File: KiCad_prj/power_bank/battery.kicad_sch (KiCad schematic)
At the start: 27 parts, among them Q1 IRFR5305, Q2 IRFR4105, Q4 BC847BS, Q5 BC857BS, U1 LM317, U3 LM337

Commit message: power_bank: dokonceny navrh schema
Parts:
- renumbered C4 to C14, C3 to C15, C2 to C16, C1 to C17, C5 to C18, C6 to C19, D1 to D2, Q4 to Q1, Q5 to Q2, Q1 to Q3, Q2 to Q4, R1 to R10, R6 to R11, R5 to R12, R9 to R13, R4 to R14, R10 to R15, R2 to R16, R8 to R17, R7 to R18, R3 to R9, RV2 to RV1, RV1 to RV2, U1 to U4
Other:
- title: (none) -> ${TITLE}
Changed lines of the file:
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@@
 	(generator_version "9.0")
 	(paper "A4")
+	(title_block
+		(title "${TITLE}")
+		(date "2026-01-15")
+		(rev "${REVISION}")
+		(comment 1 "${DESCR}")
+	)
 	(junction
 		(at 106.68 107.95)
@@
 		(dnp no)
 		(fields_autoplaced yes)
-		(property "Reference" "R7"
+		(property "Reference" "R18"
 			(at 177.8 125.7299 0)
 			(effects
@@
 			(project "power_bank"
 				(path "/43391614-883f-49dc-a949-0152c58fc2fa/9147f2e0-7dcc-462c-aa60-5310dabd00a6"
-					(reference "R7")
+					(reference "R18")
 					(unit 1)
 				)
@@
 		(dnp no)
 		(fields_autoplaced yes)
-		(property "Reference" "D1"
+		(property "Reference" "D2"
 			(at 219.71 91.4399 90)
 			(effects
@@
 			(project ""
 				(path "/43391614-883f-49dc-a949-0152c58fc2fa/9147f2e0-7dcc-462c-aa60-5310dabd00a6"
-					(reference "D1")
+					(reference "D2")
 					(unit 1)
 				)
@@
 		(dnp no)
 		(fields_autoplaced yes)
-		(property "Reference" "R3"
+		(property "Reference" "R9"
 			(at 106.68 78.74 90)
 			(effects
@@
 			(project "power_bank"
 				(path "/43391614-883f-49dc-a949-0152c58fc2fa/9147f2e0-7dcc-462c-aa60-5310dabd00a6"
-					(reference "R3")
+					(reference "R9")
 					(unit 1)
 				)
@@
 		(dnp no)
 		(fields_autoplaced yes)
-		(property "Reference" "R10"
+		(property "Reference" "R15"
 			(at 168.91 54.6099 0)
 			(effects
@@
 			(project "power_bank"
 				(path "/43391614-883f-49dc-a949-0152c58fc2fa/9147f2e0-7dcc-462c-aa60-5310dabd00a6"
-					(reference "R10")
+					(reference "R15")
 					(unit 1)
 				)
@@
 		(on_board yes)
 		(dnp no)
-		(property "Reference" "Q4"
+		(property "Reference" "Q1"
 			(at 154.94 68.5801 0)
 			(effects
@@
 			(project ""
 				(path "/43391614-883f-49dc-a949-0152c58fc2fa/9147f2e0-7dcc-462c-aa60-5310dabd00a6"
-					(reference "Q4")
+					(reference "Q1")
 					(unit 1)
 				)
@@
 		(on_board yes)
 		(dnp no)
-		(property "Reference" "C5"
+		(property "Reference" "C18"
 			(at 128.27 72.3899 0)
 			(effects
@@
 			(project "power_bank"
 				(path "/43391614-883f-49dc-a949-0152c58fc2fa/9147f2e0-7dcc-462c-aa60-5310dabd00a6"
-					(reference "C5")
+					(reference "C18")
 					(unit 1)
 				)
@@
 		(dnp no)
 		(fields_autoplaced yes)
-		(property "Reference" "U1"
+		(property "Reference" "U4"
 			(at 95.25 93.98 0)
 			(effects
@@
 			(project "power_bank"
 				(path "/43391614-883f-49dc-a949-0152c58fc2fa/9147f2e0-7dcc-462c-aa60-5310dabd00a6"
-					(reference "U1")
+					(reference "U4")
 					(unit 1)
 				)
@@
 		(dnp no)
 		(fields_autoplaced yes)
-		(property "Reference" "R1"
+		(property "Reference" "R10"
 			(at 106.68 93.98 90)
 			(effects
@@
 			(project "power_bank"
 				(path "/43391614-883f-49dc-a949-0152c58fc2fa/9147f2e0-7dcc-462c-aa60-5310dabd00a6"
-					(reference "R1")
+					(reference "R10")
 					(unit 1)
 				)
@@
 		(dnp no)
 		(fields_autoplaced yes)
-		(property "Reference" "C4"
+		(property "Reference" "C14"
 			(at 78.74 110.4899 0)
 			(effects
@@
 			(project "power_bank"
 				(path "/43391614-883f-49dc-a949-0152c58fc2fa/9147f2e0-7dcc-462c-aa60-5310dabd00a6"
-					(reference "C4")
+					(reference "C14")
 					(unit 1)
 				)
@@
 		(dnp no)
 		(fields_autoplaced yes)
-		(property "Reference" "C1"
+		(property "Reference" "C17"
 			(at 99.06 110.4899 0)
 			(effects
@@
 			(project "power_bank"
 				(path "/43391614-883f-49dc-a949-0152c58fc2fa/9147f2e0-7dcc-462c-aa60-5310dabd00a6"
-					(reference "C1")
+					(reference "C17")
 					(unit 1)
 				)
@@
 		(dnp no)
 		(fields_autoplaced yes)
-		(property "Reference" "R2"
+		(property "Reference" "R16"
 			(at 168.91 125.7299 0)
 			(effects
@@
 			(project ""
 				(path "/43391614-883f-49dc-a949-0152c58fc2fa/9147f2e0-7dcc-462c-aa60-5310dabd00a6"
-					(reference "R2")
+					(reference "R16")
 					(unit 1)
 				)
@@
 		(on_board yes)
 		(dnp no)
-		(property "Reference" "C6"
+		(property "Reference" "C19"
 			(at 128.27 110.4899 0)
 			(effects
@@
 			(project "power_bank"
 				(path "/43391614-883f-49dc-a949-0152c58fc2fa/9147f2e0-7dcc-462c-aa60-5310dabd00a6"
-					(reference "C6")
+					(reference "C19")
 					(unit 1)
 				)
@@
 		(dnp no)
 		(fields_autoplaced yes)
-		(property "Reference" "R9"
+		(property "Reference" "R13"
 			(at 160.02 54.6099 0)
 			(effects
@@
 			(project "power_bank"
 				(path "/43391614-883f-49dc-a949-0152c58fc2fa/9147f2e0-7dcc-462c-aa60-5310dabd00a6"
-					(reference "R9")
+					(reference "R13")
 					(unit 1)
 				)
@@
 		(dnp no)
 		(fields_autoplaced yes)
-		(property "Reference" "R6"
+		(property "Reference" "R11"
 			(at 113.03 80.0099 0)
 			(effects
@@
 			(project "power_bank"
 				(path "/43391614-883f-49dc-a949-0152c58fc2fa/9147f2e0-7dcc-462c-aa60-5310dabd00a6"
-					(reference "R6")
+					(reference "R11")
 					(unit 1)
 				)
@@
 		(on_board yes)
 		(dnp no)
-		(property "Reference" "Q5"
+		(property "Reference" "Q2"
 			(at 177.8 114.2999 0)
 			(effects
@@
 			(project ""
 				(path "/43391614-883f-49dc-a949-0152c58fc2fa/9147f2e0-7dcc-462c-aa60-5310dabd00a6"
-					(reference "Q5")
+					(reference "Q2")
 					(unit 2)
 				)
@@
 		(dnp no)
 		(fields_autoplaced yes)
-		(property "Reference" "R5"
+		(property "Reference" "R12"
 			(at 113.03 102.8699 0)
 			(effects
@@
 			(project "power_bank"
 				(path "/43391614-883f-49dc-a949-0152c58fc2fa/9147f2e0-7dcc-462c-aa60-5310dabd00a6"
-					(reference "R5")
+					(reference "R12")
 					(unit 1)
 				)
@@
 		(on_board yes)
 		(dnp no)
-		(property "Reference" "Q4"
+		(property "Reference" "Q1"
 			(at 177.8 68.5801 0)
 			(effects
@@
 			(project ""
 				(path "/43391614-883f-49dc-a949-0152c58fc2fa/9147f2e0-7dcc-462c-aa60-5310dabd00a6"
-					(reference "Q4")
+					(reference "Q1")
 					(unit 2)
 				)
@@
 		(dnp no)
 		(fields_autoplaced yes)
-		(property "Reference" "R8"
+		(property "Reference" "R17"
 			(at 177.8 54.6099 0)
 			(effects
@@
 			(project "power_bank"
 				(path "/43391614-883f-49dc-a949-0152c58fc2fa/9147f2e0-7dcc-462c-aa60-5310dabd00a6"
-					(reference "R8")
+					(reference "R17")
 					(unit 1)
 				)
@@
 		(dnp no)
 		(fields_autoplaced yes)
-		(property "Reference" "Q5"
+		(property "Reference" "Q2"
 			(at 154.94 114.2999 0)
 			(effects
@@
 			(project ""
 				(path "/43391614-883f-49dc-a949-0152c58fc2fa/9147f2e0-7dcc-462c-aa60-5310dabd00a6"
-					(reference "Q5")
+					(reference "Q2")
 					(unit 1)
 				)
@@
 		(dnp no)
 		(fields_autoplaced yes)
-		(property "Reference" "Q1"
+		(property "Reference" "Q3"
 			(at 199.39 45.72 90)
 			(effects
@@
 			(project ""
 				(path "/43391614-883f-49dc-a949-0152c58fc2fa/9147f2e0-7dcc-462c-aa60-5310dabd00a6"
-					(reference "Q1")
+					(reference "Q3")
 					(unit 1)
 				)
@@
 		(on_board yes)
 		(dnp no)
-		(property "Reference" "RV2"
+		(property "Reference" "RV1"
 			(at 113.03 72.3899 0)
 			(effects
@@
 			(project "power_bank"
 				(path "/43391614-883f-49dc-a949-0152c58fc2fa/9147f2e0-7dcc-462c-aa60-5310dabd00a6"
-					(reference "RV2")
+					(reference "RV1")
 					(unit 1)
 				)
@@
 		(dnp no)
 		(fields_autoplaced yes)
-		(property "Reference" "Q2"
+		(property "Reference" "Q4"
 			(at 199.39 134.62 90)
 			(effects
@@
 			(project ""
 				(path "/43391614-883f-49dc-a949-0152c58fc2fa/9147f2e0-7dcc-462c-aa60-5310dabd00a6"
-					(reference "Q2")
+					(reference "Q4")
 					(unit 1)
 				)
@@
 		(on_board yes)
 		(dnp no)
-		(property "Reference" "C3"
+		(property "Reference" "C15"
 			(at 81.28 72.3899 0)
 			(effects
@@
 			(project "power_bank"
 				(path "/43391614-883f-49dc-a949-0152c58fc2fa/9147f2e0-7dcc-462c-aa60-5310dabd00a6"
-					(reference "C3")
+					(reference "C15")
 					(unit 1)
 				)
@@
 		(dnp no)
 		(fields_autoplaced yes)
-		(property "Reference" "R4"
+		(property "Reference" "R14"
 			(at 160.02 125.7299 0)
 			(effects
@@
 			(project "power_bank"
 				(path "/43391614-883f-49dc-a949-0152c58fc2fa/9147f2e0-7dcc-462c-aa60-5310dabd00a6"
-					(reference "R4")
+					(reference "R14")
 					(unit 1)
 				)
@@
 		(dnp no)
 		(fields_autoplaced yes)
-		(property "Reference" "C2"
+		(property "Reference" "C16"
 			(at 99.06 72.3899 0)
 			(effects
@@
 			(project "power_bank"
 				(path "/43391614-883f-49dc-a949-0152c58fc2fa/9147f2e0-7dcc-462c-aa60-5310dabd00a6"
-					(reference "C2")
+					(reference "C16")
 					(unit 1)
 				)
@@
 		(on_board yes)
 		(dnp no)
-		(property "Reference" "RV1"
+		(property "Reference" "RV2"
 			(at 113.03 110.4899 0)
 			(effects
@@
 			(project "power_bank"
 				(path "/43391614-883f-49dc-a949-0152c58fc2fa/9147f2e0-7dcc-462c-aa60-5310dabd00a6"
-					(reference "RV1")
+					(reference "RV2")
 					(unit 1)
 				)

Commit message: power_bank: doplnena pouzdra
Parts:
- C14, C15, C16, C17, C18, C19: footprint (none) -> Capacitor_SMD:C_0805_2012Metric
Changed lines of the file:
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@@
 			)
 		)
-		(property "Footprint" ""
+		(property "Footprint" "Capacitor_SMD:C_0805_2012Metric"
 			(at 125.4252 77.47 0)
 			(effects
@@
 			)
 		)
-		(property "Footprint" ""
+		(property "Footprint" "Capacitor_SMD:C_0805_2012Metric"
 			(at 75.8952 115.57 0)
 			(effects
@@
 			)
 		)
-		(property "Footprint" ""
+		(property "Footprint" "Capacitor_SMD:C_0805_2012Metric"
 			(at 96.2152 115.57 0)
 			(effects
@@
 			)
 		)
-		(property "Footprint" ""
+		(property "Footprint" "Capacitor_SMD:C_0805_2012Metric"
 			(at 125.4252 115.57 0)
 			(effects
@@
 			)
 		)
-		(property "Footprint" ""
+		(property "Footprint" "Capacitor_SMD:C_0805_2012Metric"
 			(at 84.1248 77.47 0)
 			(effects
@@
 			)
 		)
-		(property "Footprint" ""
+		(property "Footprint" "Capacitor_SMD:C_0805_2012Metric"
 			(at 96.2152 77.47 0)
 			(effects

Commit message: pocatek dps
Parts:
- added TP2, TP3, TP4, TP5, TP6, TP7: TestPoint, TestPoint:TestPoint_Loop_D1.80mm_Drill1.0mm_Beaded, symbol Connector:TestPoint
- R13: renamed from R11; footprint Resistor_THT:R_Axial_DIN0207_L6.3mm_D2.5mm_P7.62mm_Horizontal -> Resistor_SMD:R_0805_2012Metric
- R14: renamed from R12; footprint Resistor_THT:R_Axial_DIN0207_L6.3mm_D2.5mm_P7.62mm_Horizontal -> Resistor_SMD:R_0805_2012Metric
- U3, U4: footprint Package_TO_SOT_THT:TO-220-3_Vertical -> Package_TO_SOT_THT:TO-220F-3_Horizontal_TabUp
- renumbered D2 to D4, R9 to R11, R10 to R12, R13 to R15, R14 to R16, R15 to R17, R16 to R18, R17 to R19, R18 to R20
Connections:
- net BAT_NEG: now also TP7.1
- net BAT_POS: now also TP4.1
- net CHA_NEG: now also TP3.1
- net CHA_POS: now also TP2.1
- net at BT1.2 (-), C18.2, D4.1 (K)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: now also TP5.1
- net at BT2.1 (+), C19.1, D4.2 (A)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: now also TP6.1

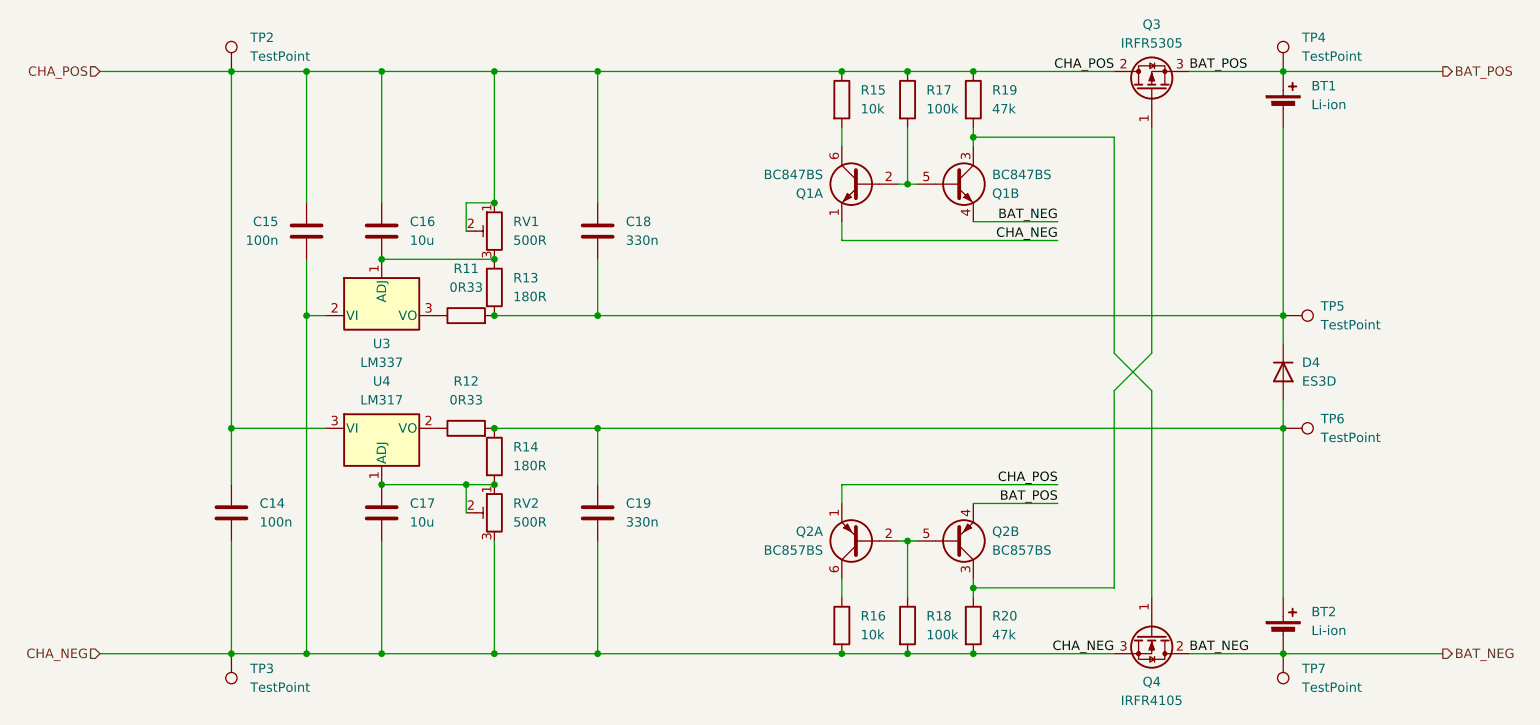
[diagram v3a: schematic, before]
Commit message: power_bank: priprava pouzdra chladice
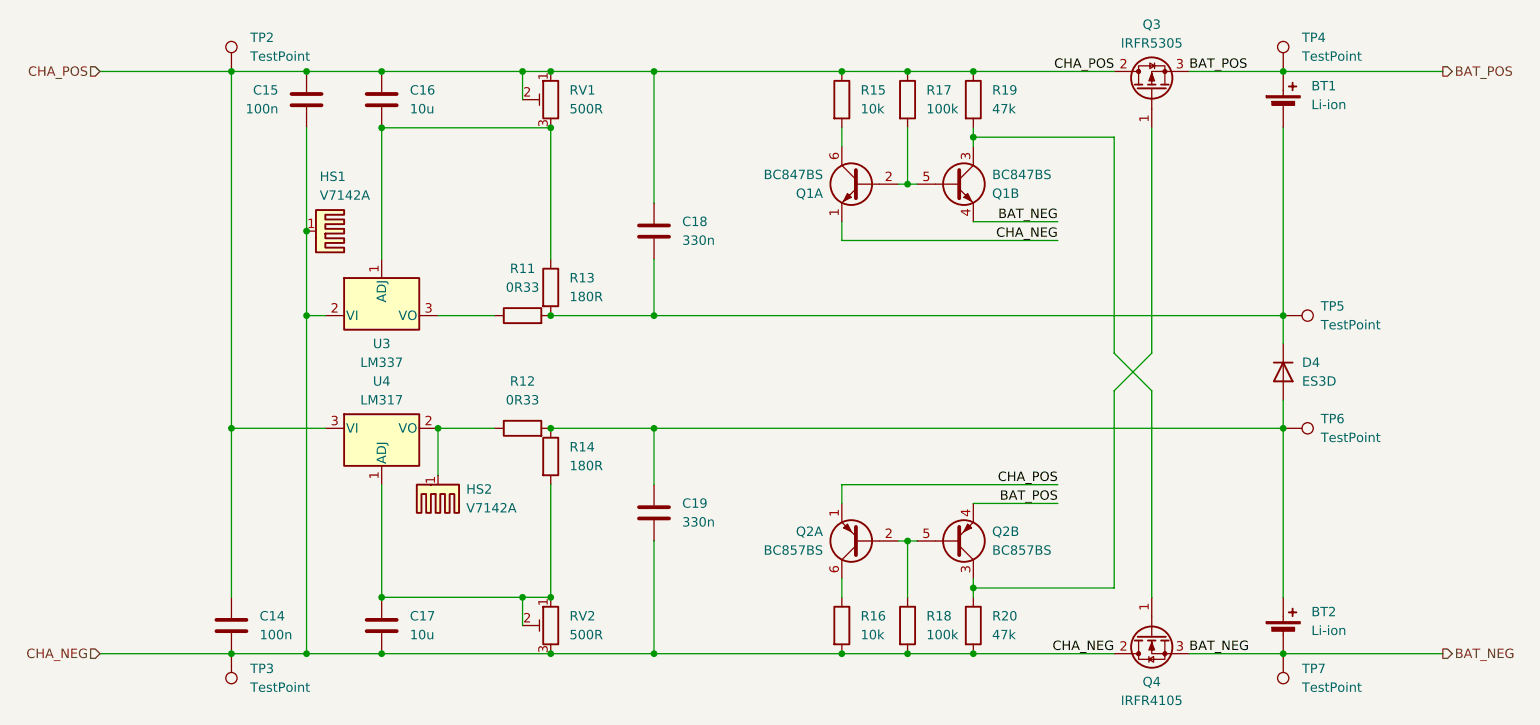
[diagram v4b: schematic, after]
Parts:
- added HS1, HS2: V7142A, heatsink:V7142A, symbol Mechanical:Heatsink_Pad
- TP2, TP3, TP4, TP5, TP6, TP7: footprint TestPoint:TestPoint_Loop_D1.80mm_Drill1.0mm_Beaded -> TestPoint:TestPoint_Pad_D2.0mm
- U3, U4: footprint Package_TO_SOT_THT:TO-220F-3_Horizontal_TabUp -> Package_TO_SOT_THT:TO-220-3_Vertical
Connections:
- net BAT_NEG: now also Q4.3 (S); no longer Q4.2 (D)
- net CHA_NEG: now also Q4.2 (D), HS1.1; no longer Q4.3 (S)
- net at R12.1, U4.2 (VO): now also HS2.1
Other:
- moved on the sheet: C14, C15, C16, C17, C18, C19, Q4, R11, R12, R13, R14, RV1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

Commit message: power_bank: zakladni vzhled DPS
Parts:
- added C20: 330n, Capacitor_SMD:C_0805_2012Metric, symbol Device:C
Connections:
- net CHA_NEG: now also C20.2
- net CHA_POS: now also C20.1
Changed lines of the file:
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@@
+	)
+	(junction
+		(at 143.51 52.07)
+		(diameter 0)
+		(color 0 0 0 0)
+	)
+	(junction
+		(at 143.51 130.81)
+		(diameter 0)
+		(color 0 0 0 0)
 	)
 	(junction
@@
 	(wire
 		(pts
+			(xy 143.51 96.52) (xy 143.51 130.81)
+		)
+		(stroke
+			(width 0)
+			(type default)
+		)
+	)
+	(wire
+		(pts
 			(xy 114.3 123.19) (xy 118.11 123.19)
 		)
@@
 	(wire
 		(pts
+			(xy 143.51 130.81) (xy 157.48 130.81)
+		)
+		(stroke
+			(width 0)
+			(type default)
+		)
+	)
+	(wire
+		(pts
 			(xy 85.09 52.07) (xy 95.25 52.07)
 		)
@@
 	(wire
 		(pts
-			(xy 132.08 52.07) (xy 157.48 52.07)
-		)
-		(stroke
-			(width 0)
-			(type default)
-		)
-	)
-	(wire
-		(pts
-			(xy 132.08 130.81) (xy 157.48 130.81)
+			(xy 132.08 52.07) (xy 143.51 52.07)
+		)
+		(stroke
+			(width 0)
+			(type default)
+		)
+	)
+	(wire
+		(pts
+			(xy 132.08 130.81) (xy 143.51 130.81)
 		)
 		(stroke
@@
 	(wire
 		(pts
+			(xy 143.51 52.07) (xy 157.48 52.07)
+		)
+		(stroke
+			(width 0)
+			(type default)
+		)
+	)
+	(wire
+		(pts
 			(xy 132.08 115.57) (xy 132.08 130.81)
 		)
@@
 		(pts
 			(xy 175.26 60.96) (xy 194.31 60.96)
+		)
+		(stroke
+			(width 0)
+			(type default)
+		)
+	)
+	(wire
+		(pts
+			(xy 143.51 52.07) (xy 143.51 88.9)
 		)
 		(stroke
@@
 					(unit 1)
 				)
+			)
+		)
+	)
+	(symbol
+		(lib_id "Device:C")
+		(at 143.51 92.71 0)
+		(unit 1)
+		(exclude_from_sim no)
+		(in_bom yes)
+		(on_board yes)
+		(dnp no)
+		(property "Reference" "C20"
+			(at 147.32 91.4399 0)
+			(effects
+				(font
+					(size 1.27 1.27)
+				)
+				(justify left)
+			)
+		)
+		(property "Value" "330n"
+			(at 147.32 93.9799 0)
+			(effects
+				(font
+					(size 1.27 1.27)
+				)
+				(justify left)
+			)
+		)
+		(property "Footprint" "Capacitor_SMD:C_0805_2012Metric"
+			(at 144.4752 96.52 0)
+			(effects
+				(font
+					(size 1.27 1.27)
+				)
+				(hide yes)
+			)
+		)
+		(property "Datasheet" "~"
+			(at 143.51 92.71 0)
+			(effects
+				(font
+					(size 1.27 1.27)
+				)
+				(hide yes)
+			)
+		)
+		(property "Description" "Unpolarized capacitor"
+			(at 143.51 92.71 0)
+			(effects
+				(font
+					(size 1.27 1.27)
+				)
+				(hide yes)
+			)
+		)
+		(pin "1"
+		)
+		(pin "2"
+		)
+		(instances
+			(project "power_bank"
+				(path "/43391614-883f-49dc-a949-0152c58fc2fa/9147f2e0-7dcc-462c-aa60-5310dabd00a6"
+					(reference "C20")
+					(unit 1)
+				)

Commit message: Odeslano do vyroby, rev 1.0
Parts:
- C14, C15: JLCPCB Part # (none) -> C28233
- C16, C17: JLCPCB Part # (none) -> C15850
- C18, C19, C20: JLCPCB Part # (none) -> C1740
- D4: JLCPCB Part # (none) -> C16235
- HS1, HS2, R11, R12, RV1, RV2, TP2, TP3, TP4, TP5, TP6, TP7, U3, U4: now left out of the parts list
- Q1: JLCPCB Part # (none) -> C8653
- Q2: JLCPCB Part # (none) -> C8654
- Q3: JLCPCB Part # (none) -> C2624
- Q4: JLCPCB Part # (none) -> C22366766
- R13, R14: JLCPCB Part # (none) -> C1339
- R15, R16: JLCPCB Part # (none) -> C17414
- R17, R18: JLCPCB Part # (none) -> C149504
- R19, R20: JLCPCB Part # (none) -> C17713
